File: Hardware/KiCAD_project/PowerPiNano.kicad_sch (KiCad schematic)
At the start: 67 parts, among them J1 SW_interface, J2 USB_B_Mini, J3 resistor network 1, J4 IOs, J5 IOs, J6 resistor network 2, Q1 MMBT3904, Q2 MMBT3904, Q3 MMBT3904, Q4 MMBT3904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

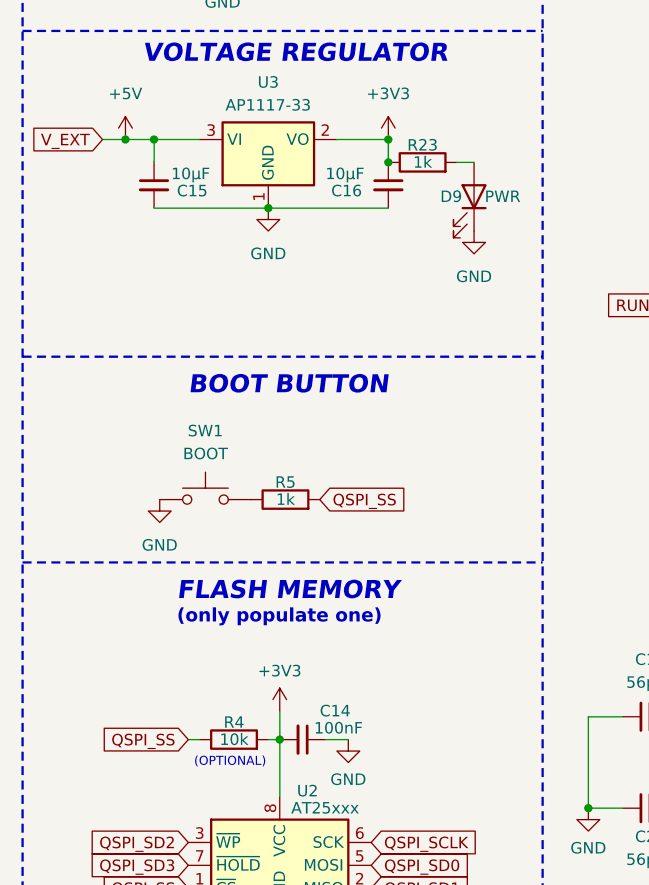
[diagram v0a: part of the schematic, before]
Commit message: replaced schematic symbols of the electrolytic caps for the correct ones
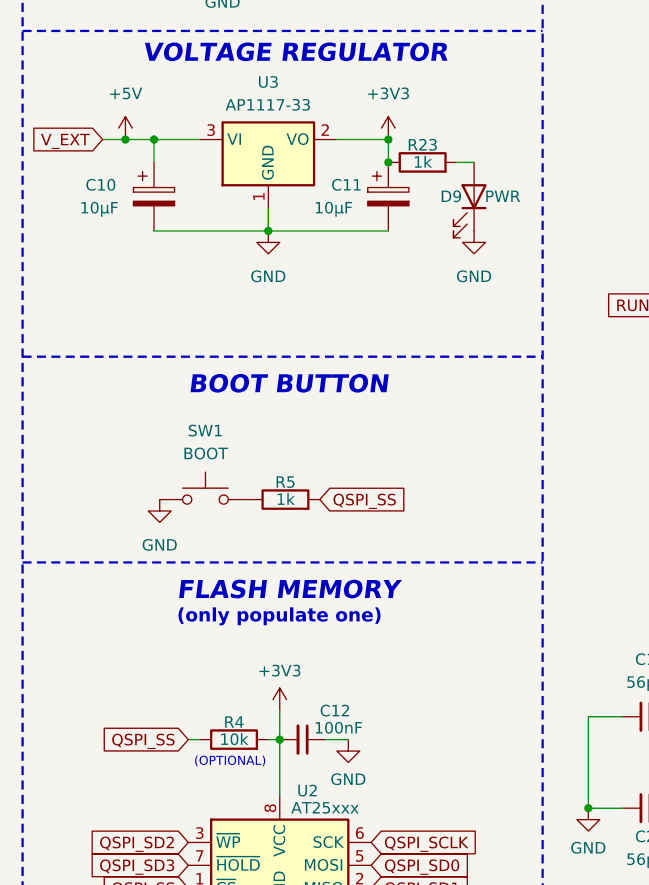
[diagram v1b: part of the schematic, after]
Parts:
- removed C15, C16: 10µF, Capacitor_SMD:CP_Elec_4x3, symbol Device:C_Small
- added C10, C11: 10µF, Capacitor_SMD:CP_Elec_4x3, symbol Device:C_Polarized
- renumbered C14 to C12
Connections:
- net +3V3: now also C11.1
- net +5V: now also C10.1
- net GND: now also C10.2, C11.2
